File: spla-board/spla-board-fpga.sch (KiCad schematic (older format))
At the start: 4 parts, among them J2 J_JTAG, U1 LFE5U-45F-BG256

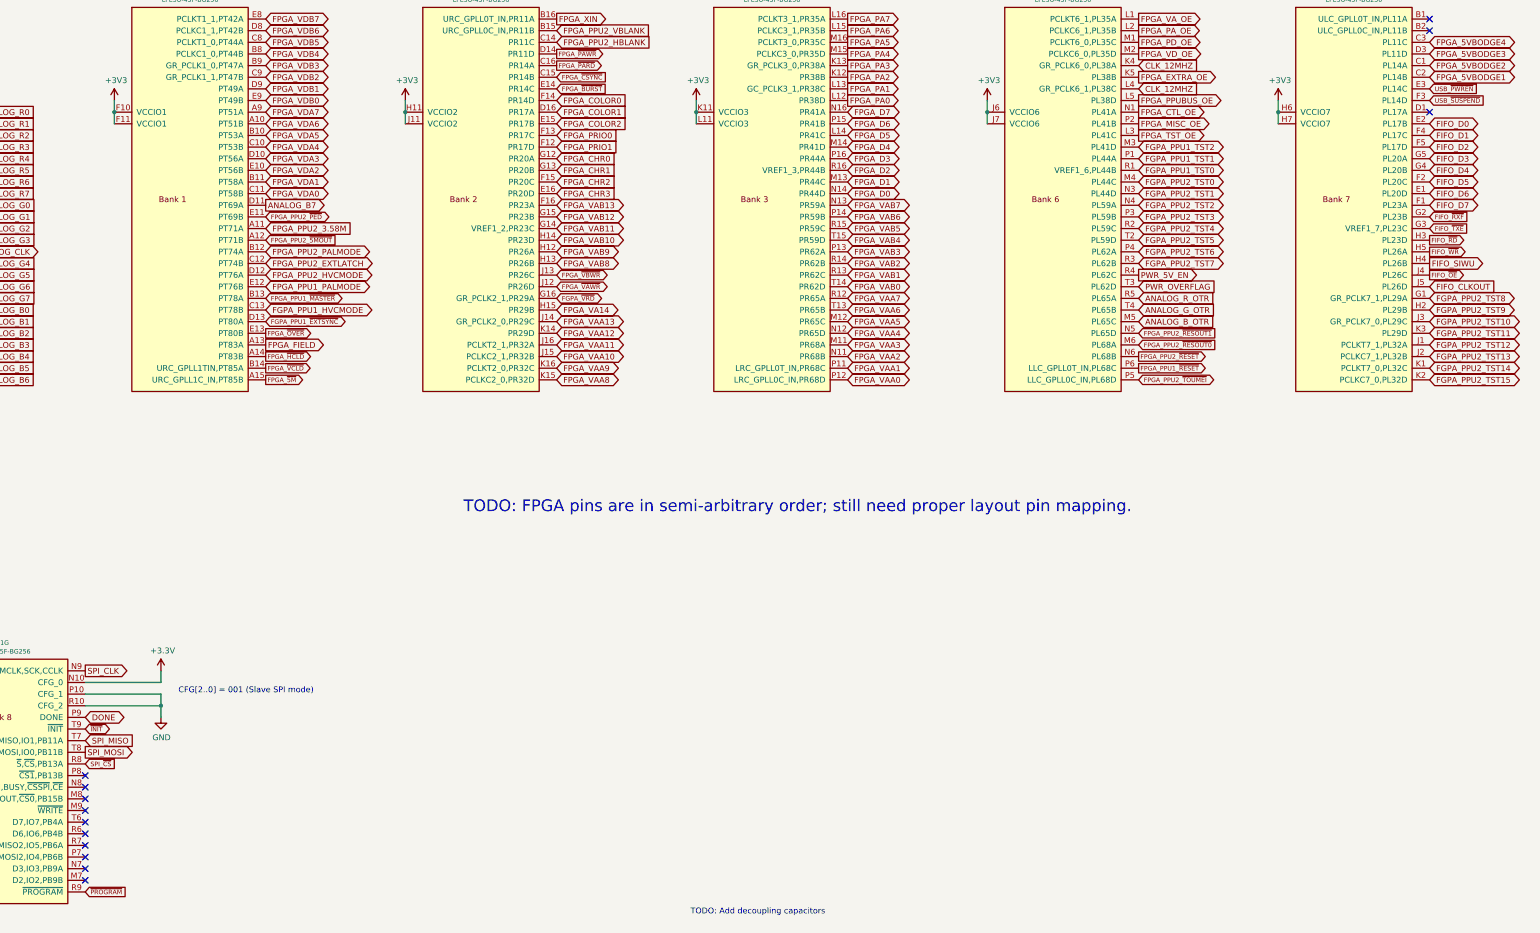
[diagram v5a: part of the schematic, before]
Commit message: pcb/schematic: Layout FPGA/FTDI so that FIFO connects are reasonable.
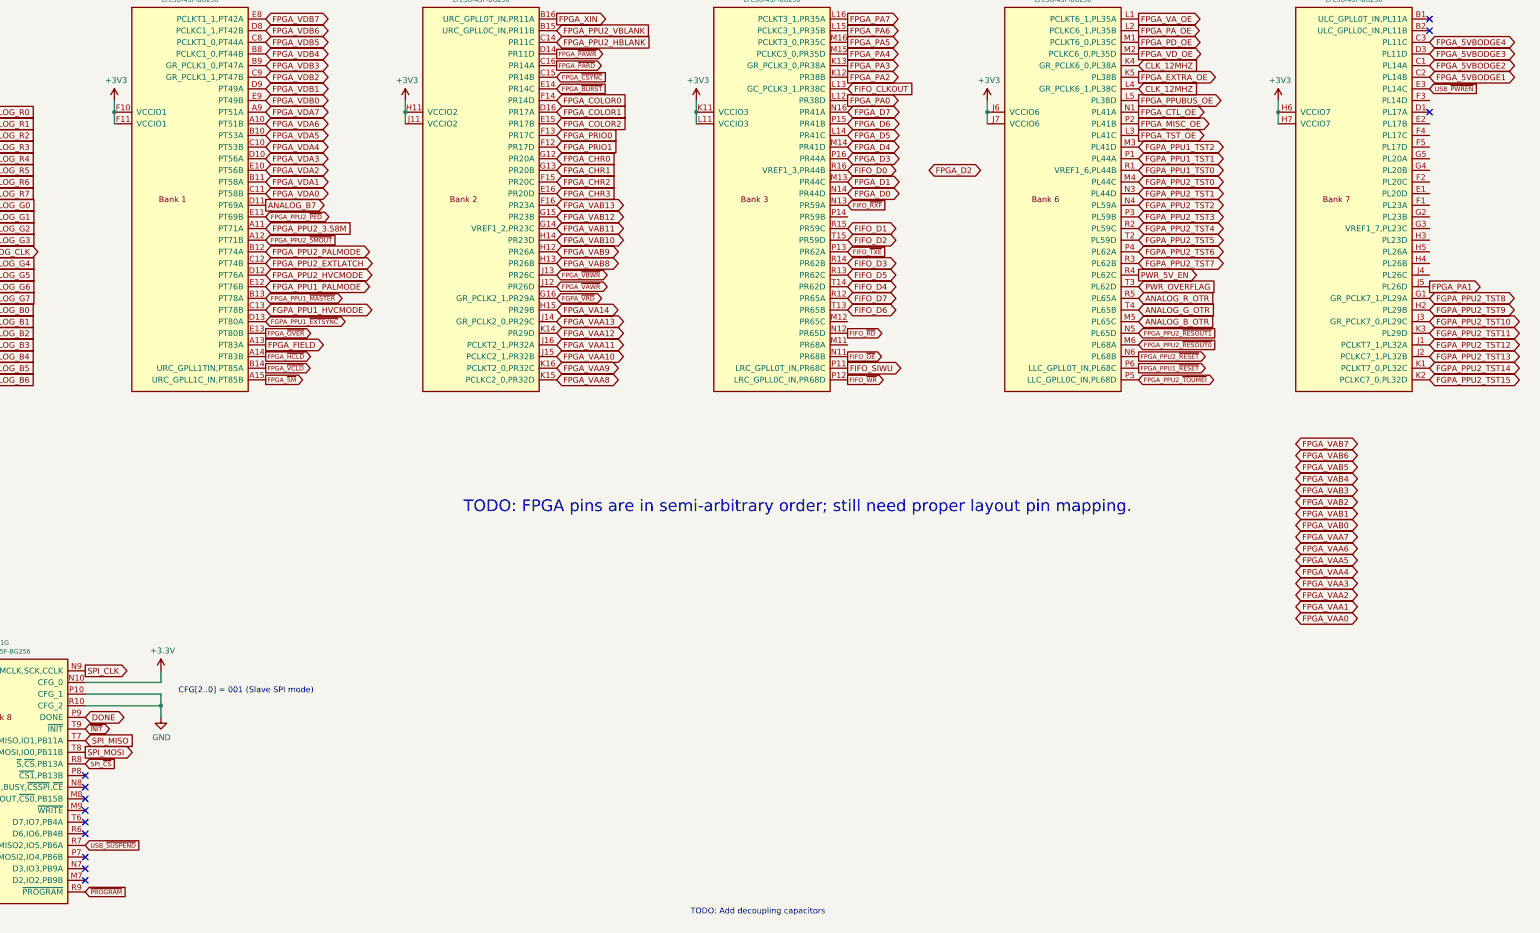
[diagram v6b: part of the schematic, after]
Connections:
- net FIFO_CLKOUT: now also U1.L13 (GC_PCLK3_1,PR38C); no longer U1.J5 (PL26D)
- net FIFO_D0: now also U1.R16 (VREF1_3,PR44B); no longer U1.E2 (PL17B)
- net FIFO_D1: now also U1.R15 (PR59C); no longer U1.F4 (PL17C)
- net FIFO_D2: now also U1.T15 (PR59D); no longer U1.F5 (PL17D)
- net FIFO_D3: now also U1.R14 (PR62B); no longer U1.G5 (PL20A)
- net FIFO_D4: now also U1.T14 (PR62D); no longer U1.G4 (PL20B)
- net FIFO_D5: now also U1.R13 (PR62C); no longer U1.F2 (PL20C)
- net FIFO_D6: now also U1.T13 (PR65B); no longer U1.E1 (PL20D)
- net FIFO_D7: now also U1.R12 (PR65A); no longer U1.F1 (PL23A)
- net FIFO_SIWU: now also U1.P11 (LRC_GPLL0T_IN,PR68C); no longer U1.H4 (PL26B)
- net FIFO_~OE~: now also U1.N11 (PR68B); no longer U1.J4 (PL26C)
- net FIFO_~RD~: now also U1.N12 (PR65D); no longer U1.H3 (PL23D)
- net FIFO_~RXF~: now also U1.N13 (PR59A); no longer U1.G2 (PL23B)
- net FIFO_~TXE~: now also U1.P13 (PR62A); no longer U1.G3 (VREF1_7,PL23C)
- net FIFO_~WR~: now also U1.P12 (LRC_GPLL0C_IN,PR68D); no longer U1.H5 (PL26A)
- net FPGA_D2: no longer U1.R16 (VREF1_3,PR44B)
- net FPGA_PA1: now also U1.J5 (PL26D); no longer U1.L13 (GC_PCLK3_1,PR38C)
- net FPGA_VAA0: no longer U1.P12 (LRC_GPLL0C_IN,PR68D)
- net FPGA_VAA1: no longer U1.P11 (LRC_GPLL0T_IN,PR68C)
- net FPGA_VAA2: no longer U1.N11 (PR68B)
- net FPGA_VAA3: no longer U1.M11 (PR68A)
- net FPGA_VAA4: no longer U1.N12 (PR65D)
- net FPGA_VAA5: no longer U1.M12 (PR65C)
- net FPGA_VAA6: no longer U1.T13 (PR65B)
- net FPGA_VAA7: no longer U1.R12 (PR65A)
- net FPGA_VAB0: no longer U1.T14 (PR62D)
- net FPGA_VAB1: no longer U1.R13 (PR62C)
- net FPGA_VAB2: no longer U1.R14 (PR62B)
- net FPGA_VAB3: no longer U1.P13 (PR62A)
- net FPGA_VAB4: no longer U1.T15 (PR59D)
- net FPGA_VAB5: no longer U1.R15 (PR59C)
- net FPGA_VAB6: no longer U1.P14 (PR59B)
- net FPGA_VAB7: no longer U1.N13 (PR59A)
- net USB_~SUSPEND~: now also U1.R7 (D5,MISO2,IO5,PB6A); no longer U1.F3 (PL14D)
- no-connect marks 13 -> 12
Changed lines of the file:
@@
 Text GLabel 9650 2700 2    50   BiDi ~ 0
 FPGA_D1
-Text GLabel 9650 2600 2    50   BiDi ~ 0
+Text GLabel 10350 2600 2    50   BiDi ~ 0
 FPGA_D2
 Text GLabel 9650 2500 2    50   BiDi ~ 0
@@
 Text GLabel 12150 1400 2    50   Output ~ 0
 FPGA_PA_OE
-Text GLabel 9650 1900 2    50   Output ~ 0
+Text GLabel 14650 3600 2    50   Output ~ 0
 FPGA_PA1
 Text GLabel 9650 1800 2    50   Output ~ 0
@@
 Text GLabel 9650 1300 2    50   Output ~ 0
 FPGA_PA7
-Text GLabel 9650 3600 2    50   BiDi ~ 0
+Text GLabel 13500 5650 2    50   BiDi ~ 0
 FPGA_VAB0
-Text GLabel 9650 3500 2    50   BiDi ~ 0
+Text GLabel 13500 5550 2    50   BiDi ~ 0
 FPGA_VAB1
-Text GLabel 9650 3400 2    50   BiDi ~ 0
+Text GLabel 13500 5450 2    50   BiDi ~ 0
 FPGA_VAB2
-Text GLabel 9650 3300 2    50   BiDi ~ 0
+Text GLabel 13500 5350 2    50   BiDi ~ 0
 FPGA_VAB3
-Text GLabel 9650 3200 2    50   BiDi ~ 0
+Text GLabel 13500 5250 2    50   BiDi ~ 0
 FPGA_VAB4
-Text GLabel 9650 3100 2    50   BiDi ~ 0
+Text GLabel 13500 5150 2    50   BiDi ~ 0
 FPGA_VAB5
-Text GLabel 9650 3000 2    50   BiDi ~ 0
+Text GLabel 13500 5050 2    50   BiDi ~ 0
 FPGA_VAB6
-Text GLabel 9650 2900 2    50   BiDi ~ 0
+Text GLabel 13500 4950 2    50   BiDi ~ 0
 FPGA_VAB7
-Text GLabel 9650 4400 2    50   BiDi ~ 0
+Text GLabel 13500 6450 2    50   BiDi ~ 0
 FPGA_VAA0
-Text GLabel 9650 4300 2    50   BiDi ~ 0
+Text GLabel 13500 6350 2    50   BiDi ~ 0
 FPGA_VAA1
-Text GLabel 9650 4200 2    50   BiDi ~ 0
+Text GLabel 13500 6250 2    50   BiDi ~ 0
 FPGA_VAA2
-Text GLabel 9650 4100 2    50   BiDi ~ 0
+Text GLabel 13500 6150 2    50   BiDi ~ 0
 FPGA_VAA3
-Text GLabel 9650 4000 2    50   BiDi ~ 0
+Text GLabel 13500 6050 2    50   BiDi ~ 0
 FPGA_VAA4
-Text GLabel 9650 3900 2    50   BiDi ~ 0
+Text GLabel 13500 5950 2    50   BiDi ~ 0
 FPGA_VAA5
-Text GLabel 9650 3800 2    50   BiDi ~ 0
+Text GLabel 13500 5850 2    50   BiDi ~ 0
 FPGA_VAA6
-Text GLabel 9650 3700 2    50   BiDi ~ 0
+Text GLabel 13500 5750 2    50   BiDi ~ 0
 FPGA_VAA7
 Text GLabel 7150 4400 2    50   BiDi ~ 0
@@
 Text GLabel 3100 7700 2    39   Input ~ 0
 SPI_~CS~
-Text GLabel 14650 3000 2    39   Input ~ 0
+Text GLabel 9650 2900 2    39   Input ~ 0
 FIFO_~RXF~
-Text GLabel 14650 3100 2    39   Input ~ 0
+Text GLabel 9650 3300 2    39   Input ~ 0
 FIFO_~TXE~
-Text GLabel 14650 3200 2    39   Output ~ 0
+Text GLabel 9650 4000 2    39   Output ~ 0
 FIFO_~RD~
-Text GLabel 14650 3300 2    39   Output ~ 0
+Text GLabel 9650 4400 2    39   Output ~ 0
 FIFO_~WR~
-Text GLabel 14650 3600 2    50   Input ~ 0
+Text GLabel 9650 1900 2    50   Input ~ 0
 FIFO_CLKOUT
-Text GLabel 14650 3500 2    39   Output ~ 0
+Text GLabel 9650 4200 2    39   Output ~ 0
 FIFO_~OE~
-Text GLabel 14650 3400 2    50   Output ~ 0
+Text GLabel 9650 4300 2    50   Output ~ 0
 FIFO_SIWU
-Text GLabel 14650 2900 2    50   BiDi ~ 0
+Text GLabel 9650 3700 2    50   BiDi ~ 0
 FIFO_D7
-Text GLabel 14650 2800 2    50   BiDi ~ 0
+Text GLabel 9650 3800 2    50   BiDi ~ 0
 FIFO_D6
-Text GLabel 14650 2700 2    50   BiDi ~ 0
+Text GLabel 9650 3500 2    50   BiDi ~ 0
 FIFO_D5
-Text GLabel 14650 2600 2    50   BiDi ~ 0
+Text GLabel 9650 3600 2    50   BiDi ~ 0
 FIFO_D4
-Text GLabel 14650 2500 2    50   BiDi ~ 0
+Text GLabel 9650 3400 2    50   BiDi ~ 0
 FIFO_D3
-Text GLabel 14650 2400 2    50   BiDi ~ 0
+Text GLabel 9650 3200 2    50   BiDi ~ 0
 FIFO_D2
-Text GLabel 14650 2300 2    50   BiDi ~ 0
+Text GLabel 9650 3100 2    50   BiDi ~ 0
 FIFO_D1
-Text GLabel 14650 2200 2    50   BiDi ~ 0
+Text GLabel 9650 2600 2    50   BiDi ~ 0
 FIFO_D0
 Text Notes 3900 7100 0    50   ~ 0
@@
 NoConn ~ 3100 8200
 NoConn ~ 3100 8300
-NoConn ~ 3100 8400
 NoConn ~ 3100 8500
 NoConn ~ 3100 8600
@@
 Text GLabel 14650 1900 2    39   Input ~ 0
 USB_~PWREN~
-Text GLabel 14650 2000 2    39   Input ~ 0
+Text GLabel 3100 8400 2    39   Input ~ 0
 USB_~SUSPEND~
 $EndSCHEMATC

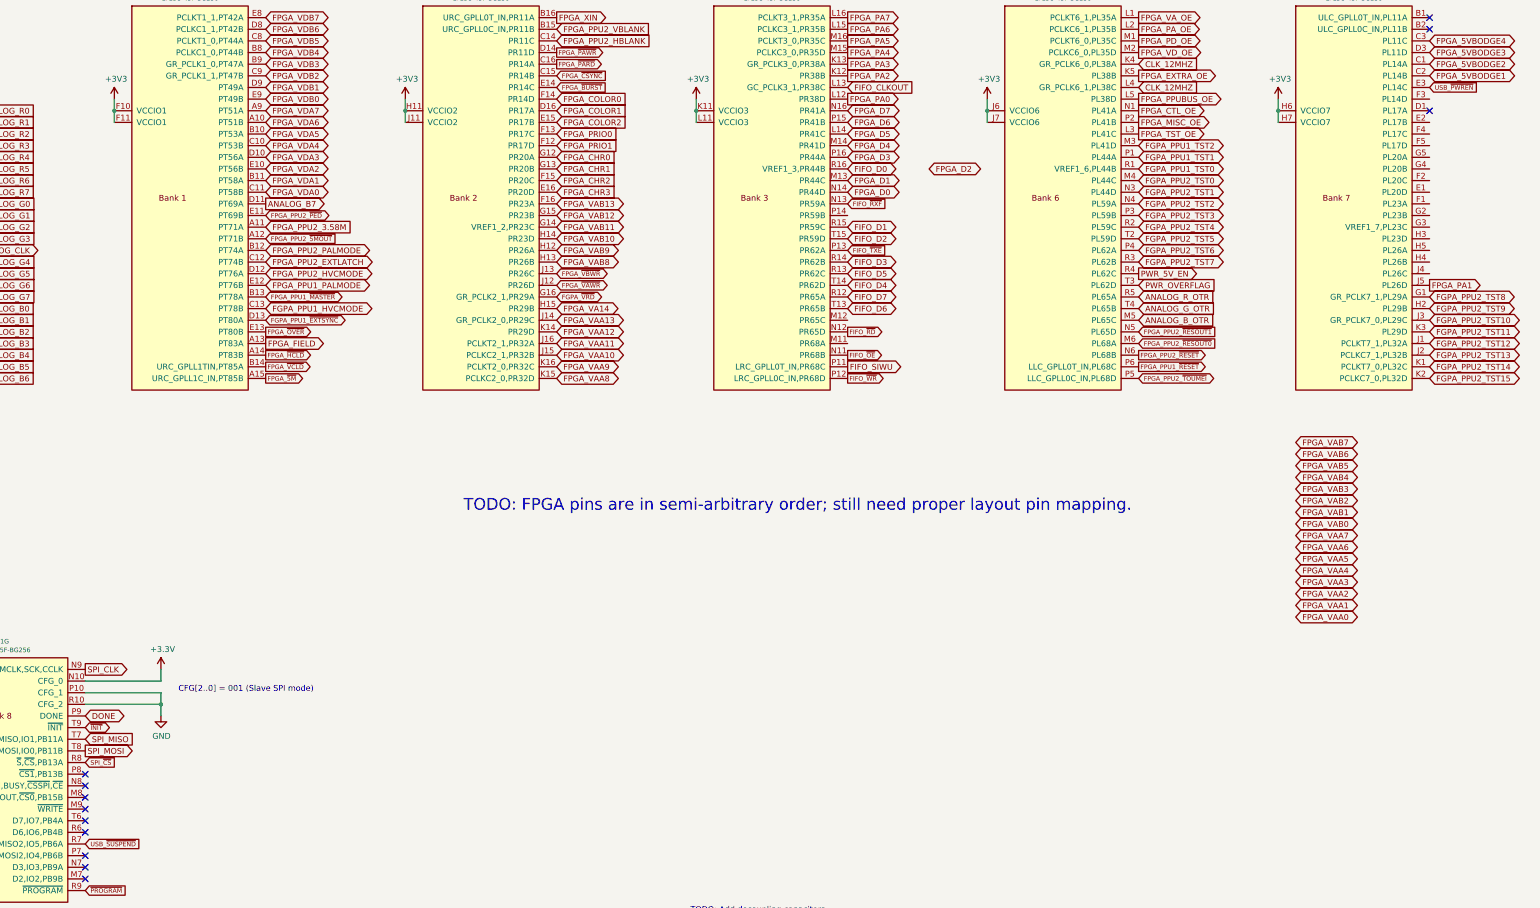
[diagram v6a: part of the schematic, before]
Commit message: pcb/schematic: Name several FTDI lines; related tweaks.
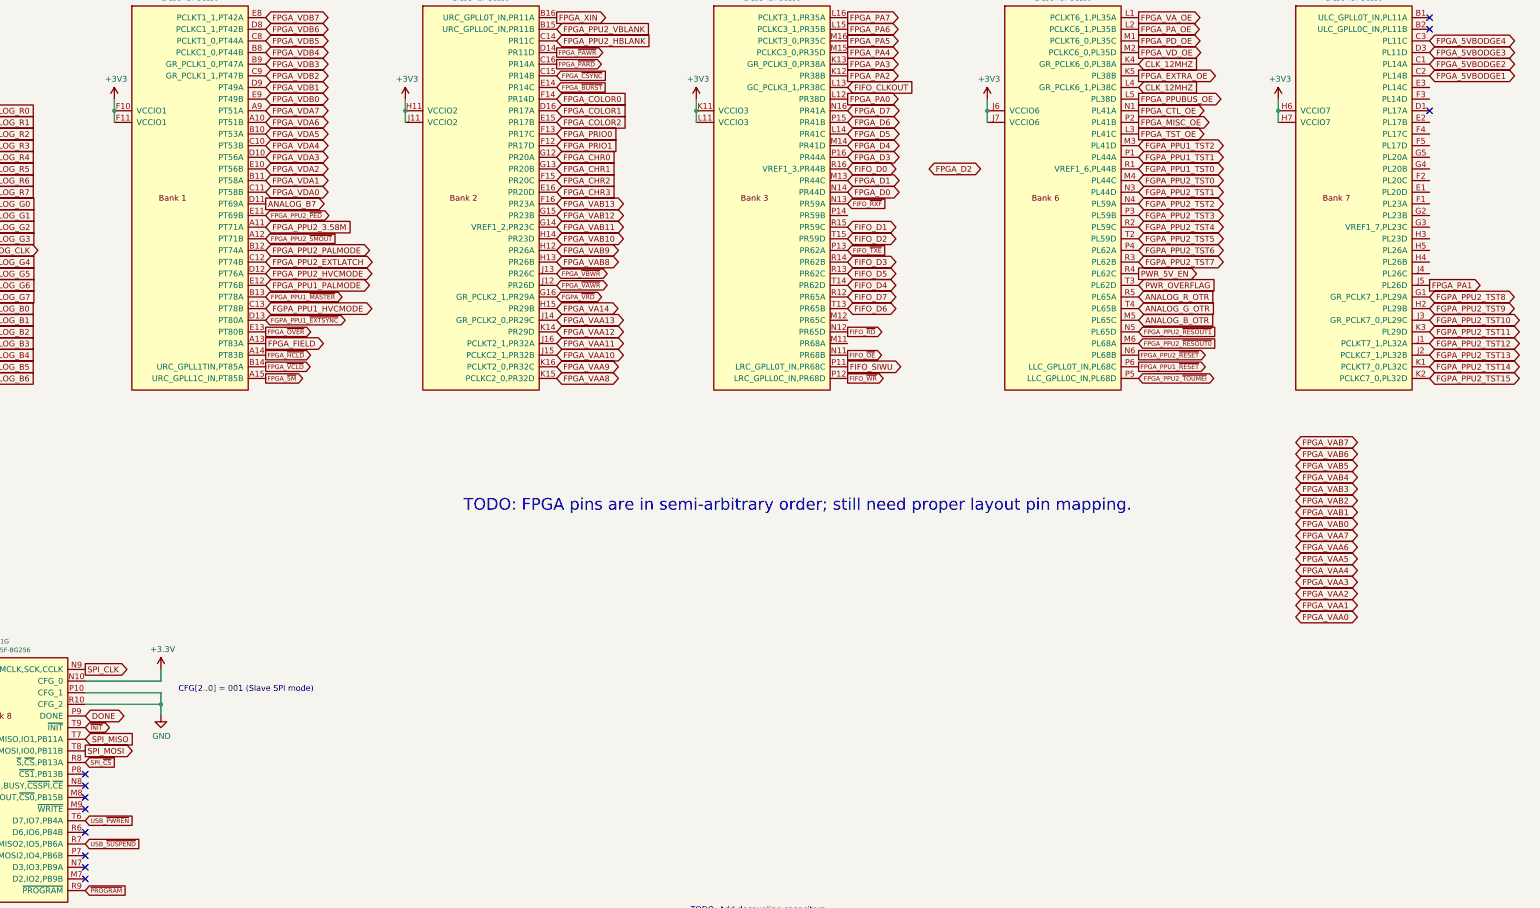
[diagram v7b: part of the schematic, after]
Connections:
- net USB_~PWREN~: now also U1.T6 (D7,IO7,PB4A); no longer U1.E3 (PL14C)
- no-connect marks 12 -> 11
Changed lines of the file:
@@
 NoConn ~ 3100 8000
 NoConn ~ 3100 8100
-NoConn ~ 3100 8200
 NoConn ~ 3100 8300
 NoConn ~ 3100 8500
@@
 FGPA_PPU2_TST0
 NoConn ~ 14650 2100
-Text GLabel 14650 1900 2    39   Input ~ 0
+Text GLabel 3100 8200 2    39   Input ~ 0
 USB_~PWREN~
 Text GLabel 3100 8400 2    39   Input ~ 0
